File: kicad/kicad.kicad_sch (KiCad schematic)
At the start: 12 parts, among them SW102 PWR_SWITCH

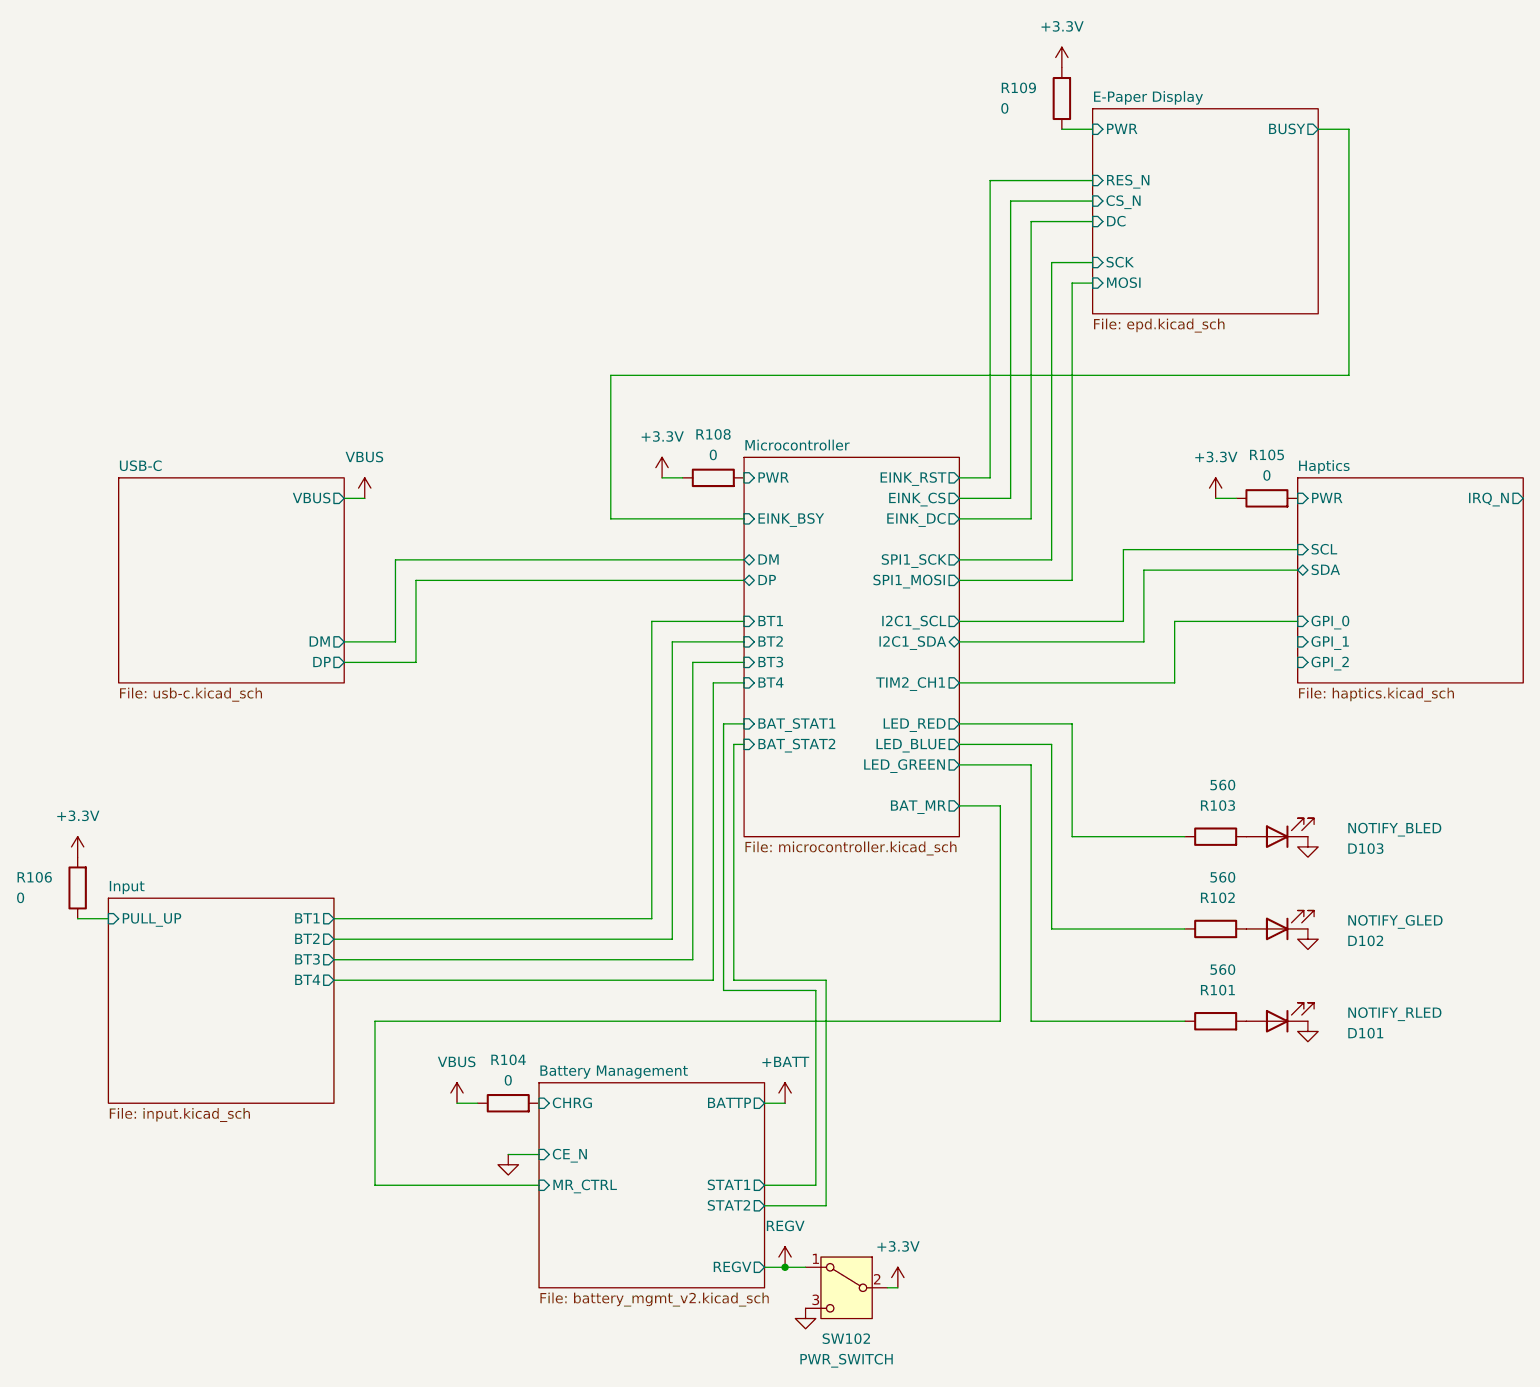
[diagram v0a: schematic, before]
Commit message: Small switch updates and fixes
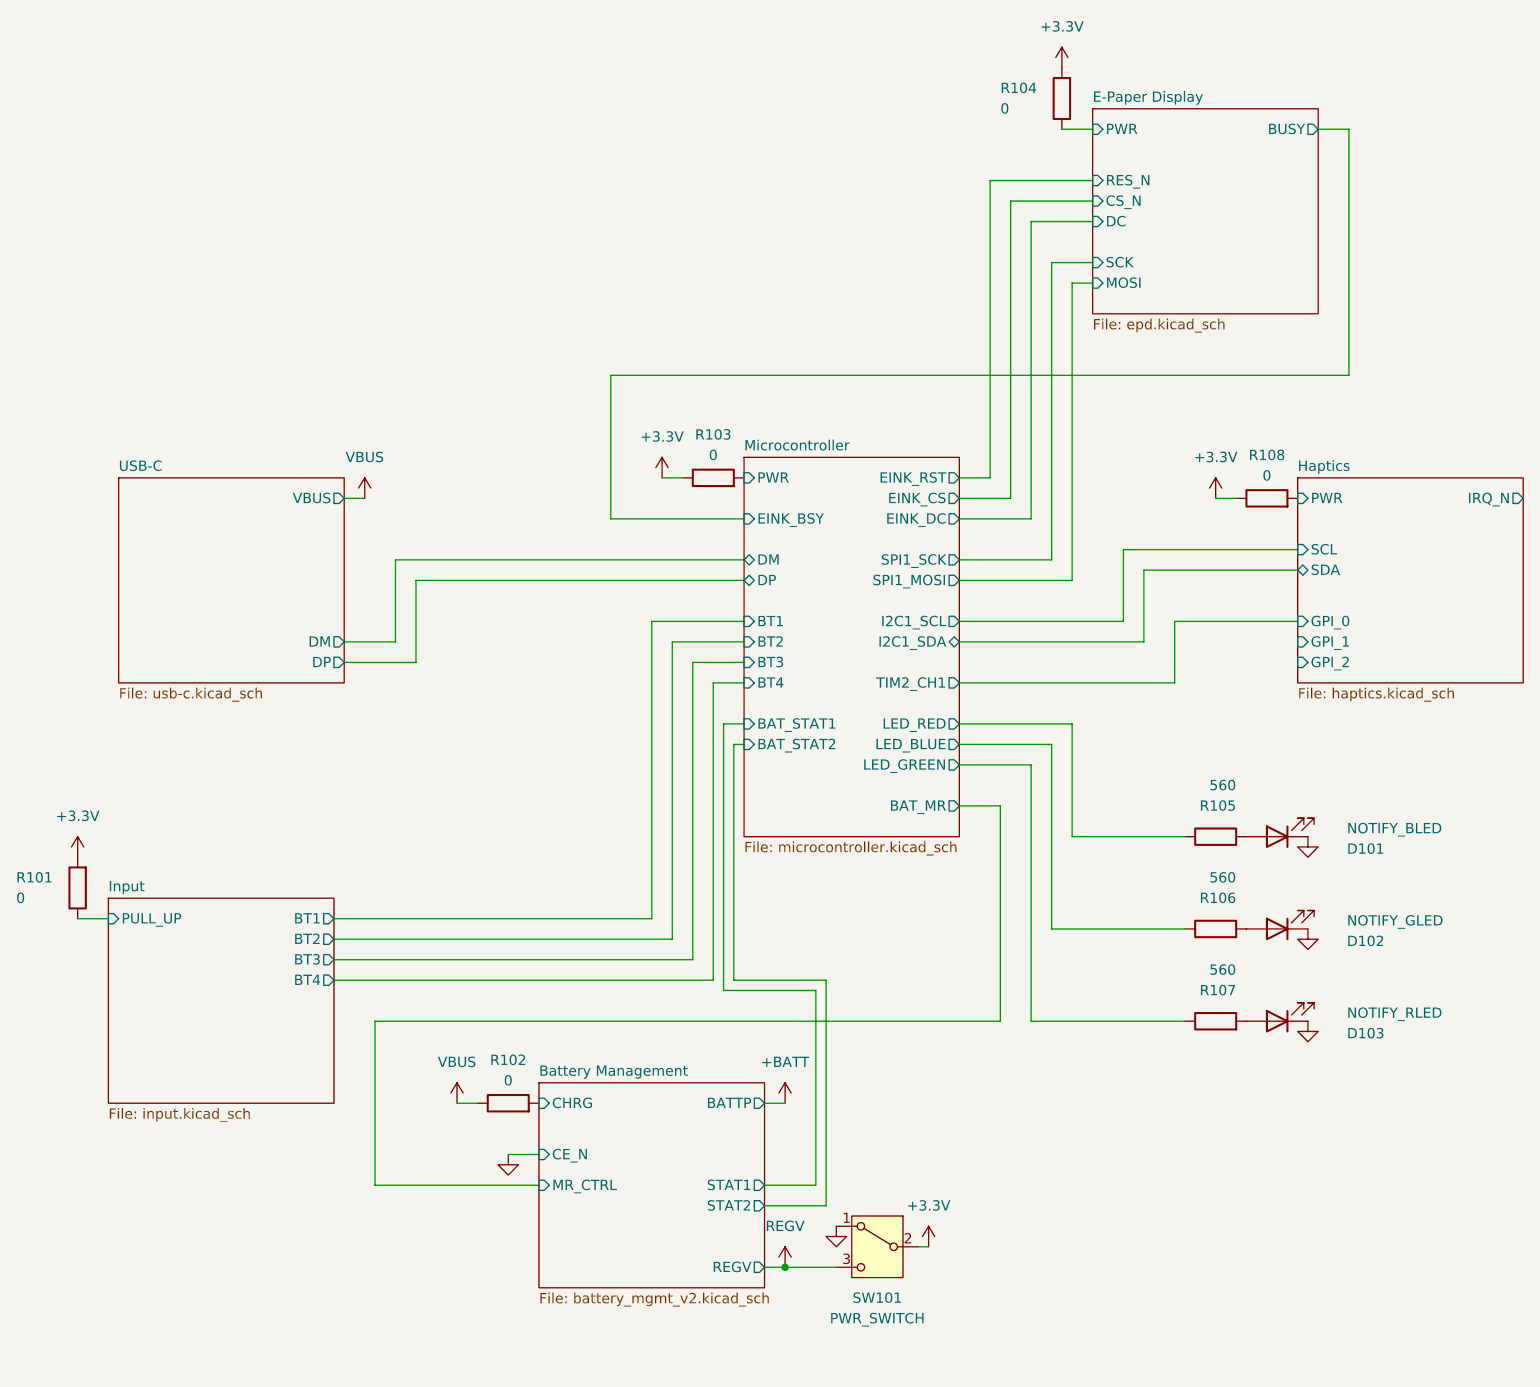
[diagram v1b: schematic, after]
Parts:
- renumbered D103 to D101, D101 to D103, R106 to R101, R104 to R102, R108 to R103, R109 to R104, R103 to R105, R102 to R106, R101 to R107, R105 to R108, SW102 to SW101
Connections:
- net GND: now also SW101.1 (A); no longer SW101.3 (C)
- net REGV: now also SW101.3 (C); no longer SW101.1 (A)
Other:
- moved on the sheet: SW101

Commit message: Part updates
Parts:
- R101, R103, R104, R108: footprint (none) -> Resistor_SMD:R_0603_1608Metric_Pad0.98x0.95mm_HandSolder
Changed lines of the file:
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@@
 			)
 		)
-		(property "Footprint" ""
+		(property "Footprint" "Resistor_SMD:R_0603_1608Metric_Pad0.98x0.95mm_HandSolder"
 			(at 116.84 83.058 90)
 			(effects
@@
 			)
 		)
-		(property "Footprint" ""
+		(property "Footprint" "Resistor_SMD:R_0603_1608Metric_Pad0.98x0.95mm_HandSolder"
 			(at 185.42 85.598 90)
 			(effects
@@
 			)
 		)
-		(property "Footprint" ""
+		(property "Footprint" "Resistor_SMD:R_0603_1608Metric_Pad0.98x0.95mm_HandSolder"
 			(at 161.798 34.29 90)
 			(effects
@@
 			)
 		)
-		(property "Footprint" ""
+		(property "Footprint" "Resistor_SMD:R_0603_1608Metric_Pad0.98x0.95mm_HandSolder"
 			(at 39.878 132.08 90)
 			(effects

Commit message: Finish microcontroller power supply
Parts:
- R102: footprint Raven:JS102000SAQN -> Resistor_SMD:R_0603_1608Metric_Pad0.98x0.95mm_HandSolder
- SW101: footprint Raven:JS102000SAQN -> Raven:SSSS811101
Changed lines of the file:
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@@
 			)
 		)
-		(property "Footprint" "Raven:JS102000SAQN"
+		(property "Footprint" "Resistor_SMD:R_0603_1608Metric_Pad0.98x0.95mm_HandSolder"
 			(at 91.44 160.528 90)
 			(effects
@@
 			)
 		)
-		(property "Footprint" "Raven:JS102000SAQN"
+		(property "Footprint" "Raven:SSSS811101"
 			(at 137.16 176.53 0)
 			(effects

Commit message: Begin PCB, update footprints
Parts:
- D101, D102, D103: footprint Diode_SMD:D_0603_1608Metric_Pad1.05x0.95mm_HandSolder -> Diode_SMD:D_0603_1608Metric
- R101, R102, R103, R104, R105, R106, R107, R108: footprint Resistor_SMD:R_0603_1608Metric_Pad0.98x0.95mm_HandSolder -> Resistor_SMD:R_0402_1005Metric
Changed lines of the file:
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@@
 			)
 		)
-		(property "Footprint" "Resistor_SMD:R_0603_1608Metric_Pad0.98x0.95mm_HandSolder"
+		(property "Footprint" "Resistor_SMD:R_0402_1005Metric"
 			(at 179.07 127.508 90)
 			(effects
@@
 			)
 		)
-		(property "Footprint" "Resistor_SMD:R_0603_1608Metric_Pad0.98x0.95mm_HandSolder"
+		(property "Footprint" "Resistor_SMD:R_0402_1005Metric"
 			(at 116.84 83.058 90)
 			(effects
@@
 			)
 		)
-		(property "Footprint" "Resistor_SMD:R_0603_1608Metric_Pad0.98x0.95mm_HandSolder"
+		(property "Footprint" "Resistor_SMD:R_0402_1005Metric"
 			(at 185.42 85.598 90)
 			(effects
@@
 			)
 		)
-		(property "Footprint" "Resistor_SMD:R_0603_1608Metric_Pad0.98x0.95mm_HandSolder"
+		(property "Footprint" "Resistor_SMD:R_0402_1005Metric"
 			(at 161.798 34.29 90)
 			(effects
@@
 			)
 		)
-		(property "Footprint" "Diode_SMD:D_0603_1608Metric_Pad1.05x0.95mm_HandSolder"
+		(property "Footprint" "Diode_SMD:D_0603_1608Metric"
 			(at 186.69 125.73 0)
 			(effects
@@
 			)
 		)
-		(property "Footprint" "Resistor_SMD:R_0603_1608Metric_Pad0.98x0.95mm_HandSolder"
+		(property "Footprint" "Resistor_SMD:R_0402_1005Metric"
 			(at 91.44 160.528 90)
 			(effects
@@
 			)
 		)
-		(property "Footprint" "Resistor_SMD:R_0603_1608Metric_Pad0.98x0.95mm_HandSolder"
+		(property "Footprint" "Resistor_SMD:R_0402_1005Metric"
 			(at 179.07 138.938 90)
 			(effects
@@
 			)
 		)
-		(property "Footprint" "Diode_SMD:D_0603_1608Metric_Pad1.05x0.95mm_HandSolder"
+		(property "Footprint" "Diode_SMD:D_0603_1608Metric"
 			(at 186.69 137.16 0)
 			(effects
@@
 			)
 		)
-		(property "Footprint" "Resistor_SMD:R_0603_1608Metric_Pad0.98x0.95mm_HandSolder"
+		(property "Footprint" "Resistor_SMD:R_0402_1005Metric"
 			(at 39.878 132.08 90)
 			(effects
@@
 			)
 		)
-		(property "Footprint" "Resistor_SMD:R_0603_1608Metric_Pad0.98x0.95mm_HandSolder"
+		(property "Footprint" "Resistor_SMD:R_0402_1005Metric"
 			(at 179.07 150.368 90)
 			(effects
@@
 			)
 		)
-		(property "Footprint" "Diode_SMD:D_0603_1608Metric_Pad1.05x0.95mm_HandSolder"
+		(property "Footprint" "Diode_SMD:D_0603_1608Metric"
 			(at 186.69 148.59 0)
 			(effects

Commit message: PCB progress
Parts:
- added D101: LED_PWR, Diode_SMD:D_0603_1608Metric, symbol Device:LED
- added R105: 560, Resistor_SMD:R_0402_1005Metric, symbol Device:R
- D102: renamed from D101; value NOTIFY_BLED -> LED_BATT
- D103: renamed from D102; value NOTIFY_GLED -> LED_F1
- D104: renamed from D103; value NOTIFY_RLED -> LED_F2
- renumbered R105 to R106, R106 to R107, R107 to R108, R108 to R109
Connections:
- net GND: now also D101.1 (K)
- net Microcontroller/LED_BLUE renamed Microcontroller/LED_F1
- net Microcontroller/LED_GREEN renamed Microcontroller/LED_F2
- net Microcontroller/LED_RED renamed Microcontroller/LED_BATT
- new net: D101.2 (A), R105.2
- new net +3V3: R105.1
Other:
- sheet Microcontroller ports: added LED_BATT, LED_F1, LED_F2; removed LED_BLUE, LED_GREEN, LED_RED

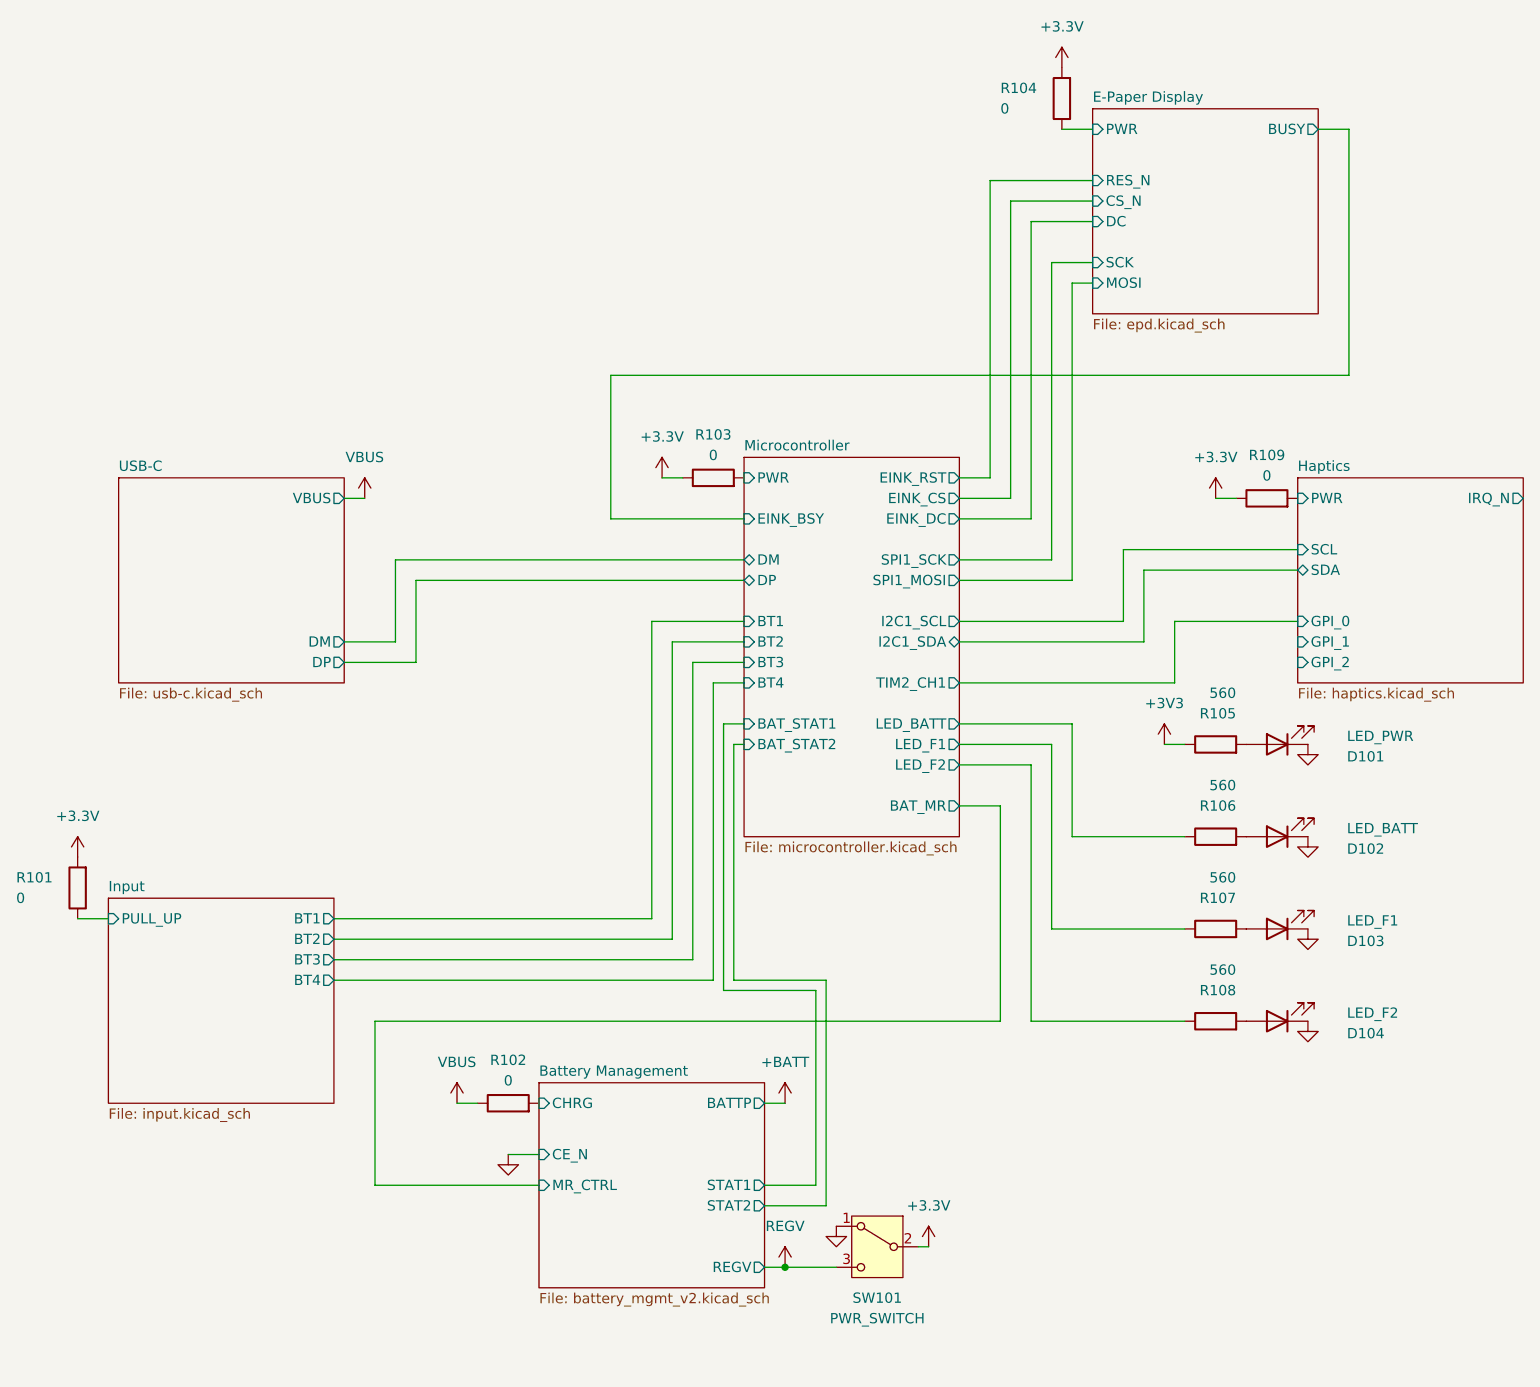
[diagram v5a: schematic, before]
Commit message: Finish PCB component placement
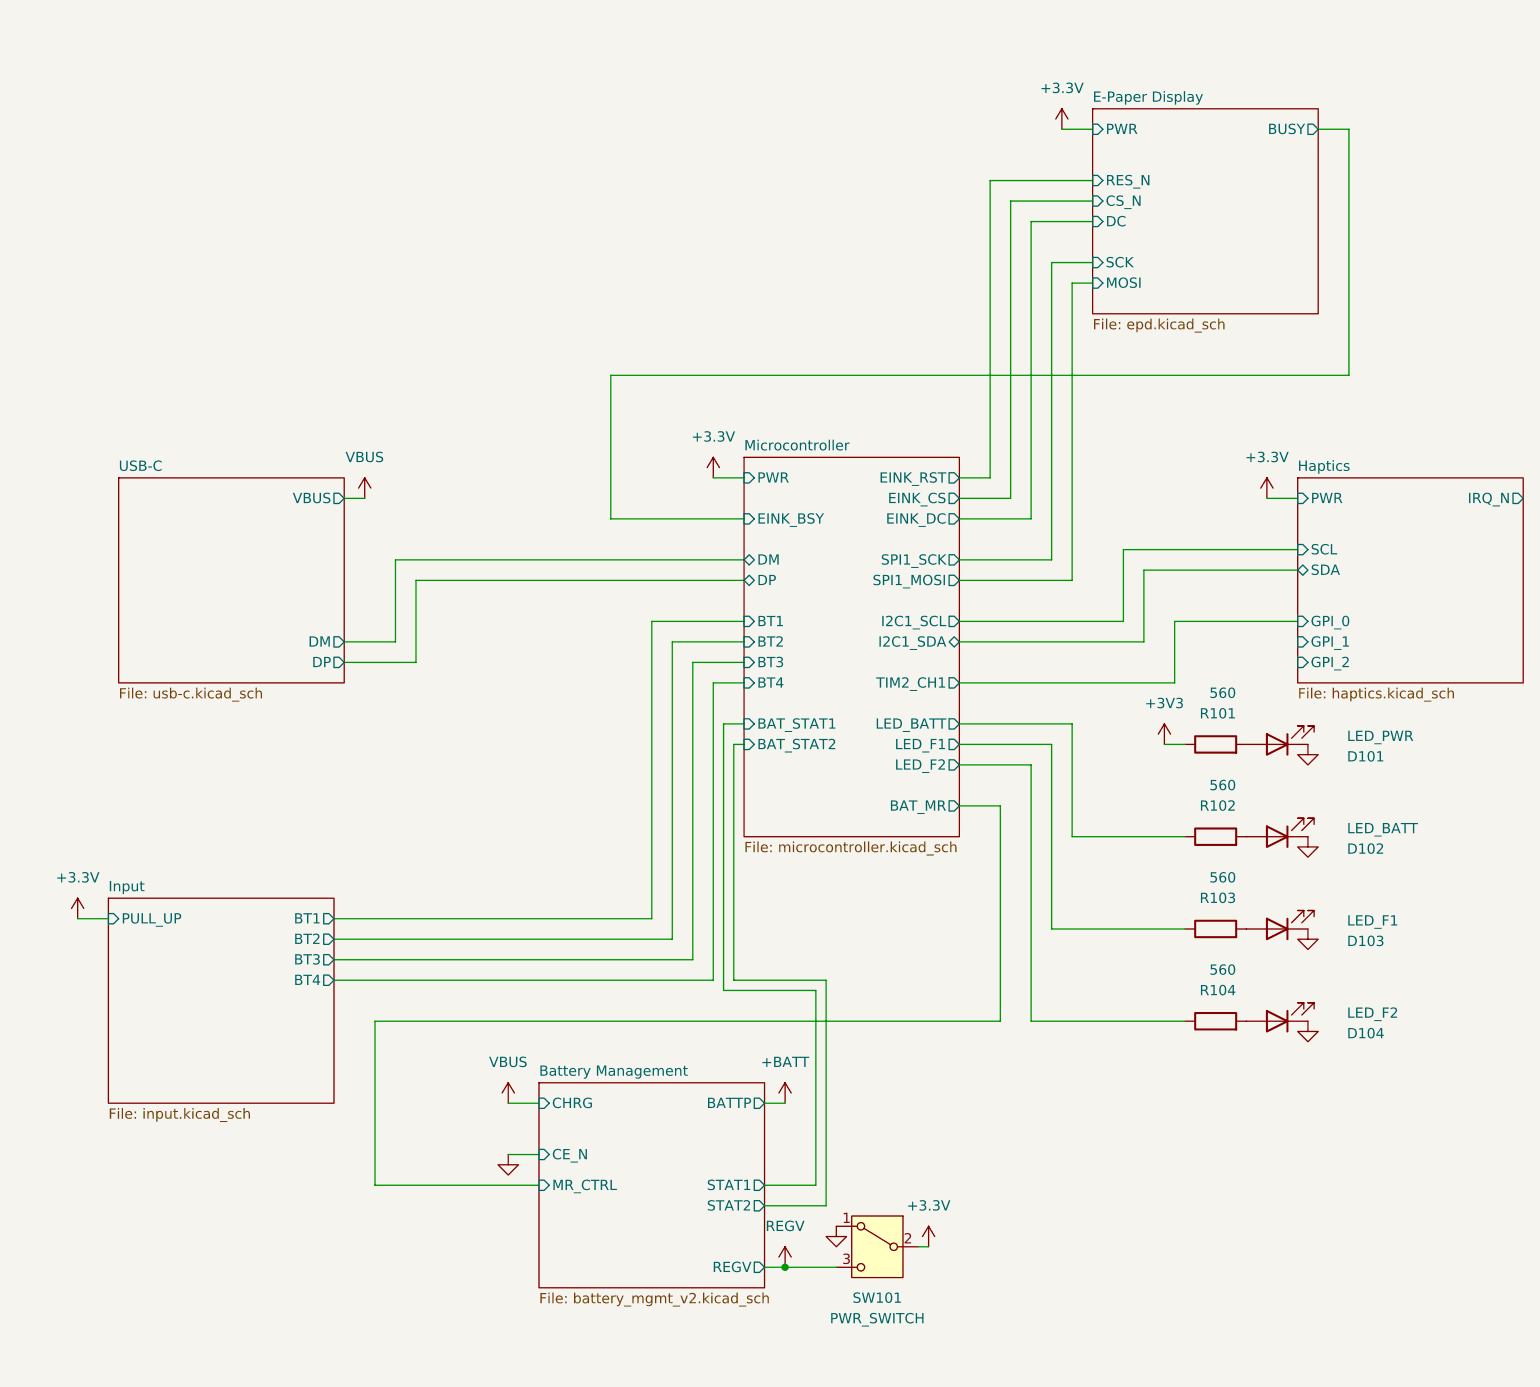
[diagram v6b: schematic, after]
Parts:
- removed R101, R102, R103, R104, R109: 0, Resistor_SMD:R_0402_1005Metric, symbol Device:R
- renumbered R105 to R101, R106 to R102, R107 to R103, R108 to R104
